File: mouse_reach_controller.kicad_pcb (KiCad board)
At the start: 2 copper layers, 158.8 x 57.2 mm, 83 parts, among them J1 AUDIO_JACK_3.5MM, P1 BNC_DOUBLE_RA, P2 BNC_DOUBLE_RA, P3 HEADER_02X05_LATCH, P4 HEADER_02X05_LATCH, P5 HEADER_02X05_LATCH, P6 PWR_JACK_2.1x5.5_SMD_RA, P7 BNC_DOUBLE_RA, T1 TERM_BLK_HDR_2POS_90DEG_0.2IN, T2 TERM_BLK_HDR_4POS_90DEG_0.2IN, U1 TMC429, U10 SGTL5000, U11 TMC424, U12 74LVC1G125GS, U13 74LVC1G125GS, U14 74LVC1G125GS, U15 74LVC1G125GS, U2 SN65LVDM050QDRQ1, U3 74LVC1G125GS, U4 SN65LVDM050QDRQ1, U5 74LVC1G125GS, U6 SN65LVDM050QDRQ1, U7 74LVC1G125GS, U8 DRV103, U9 RT9076-15GV

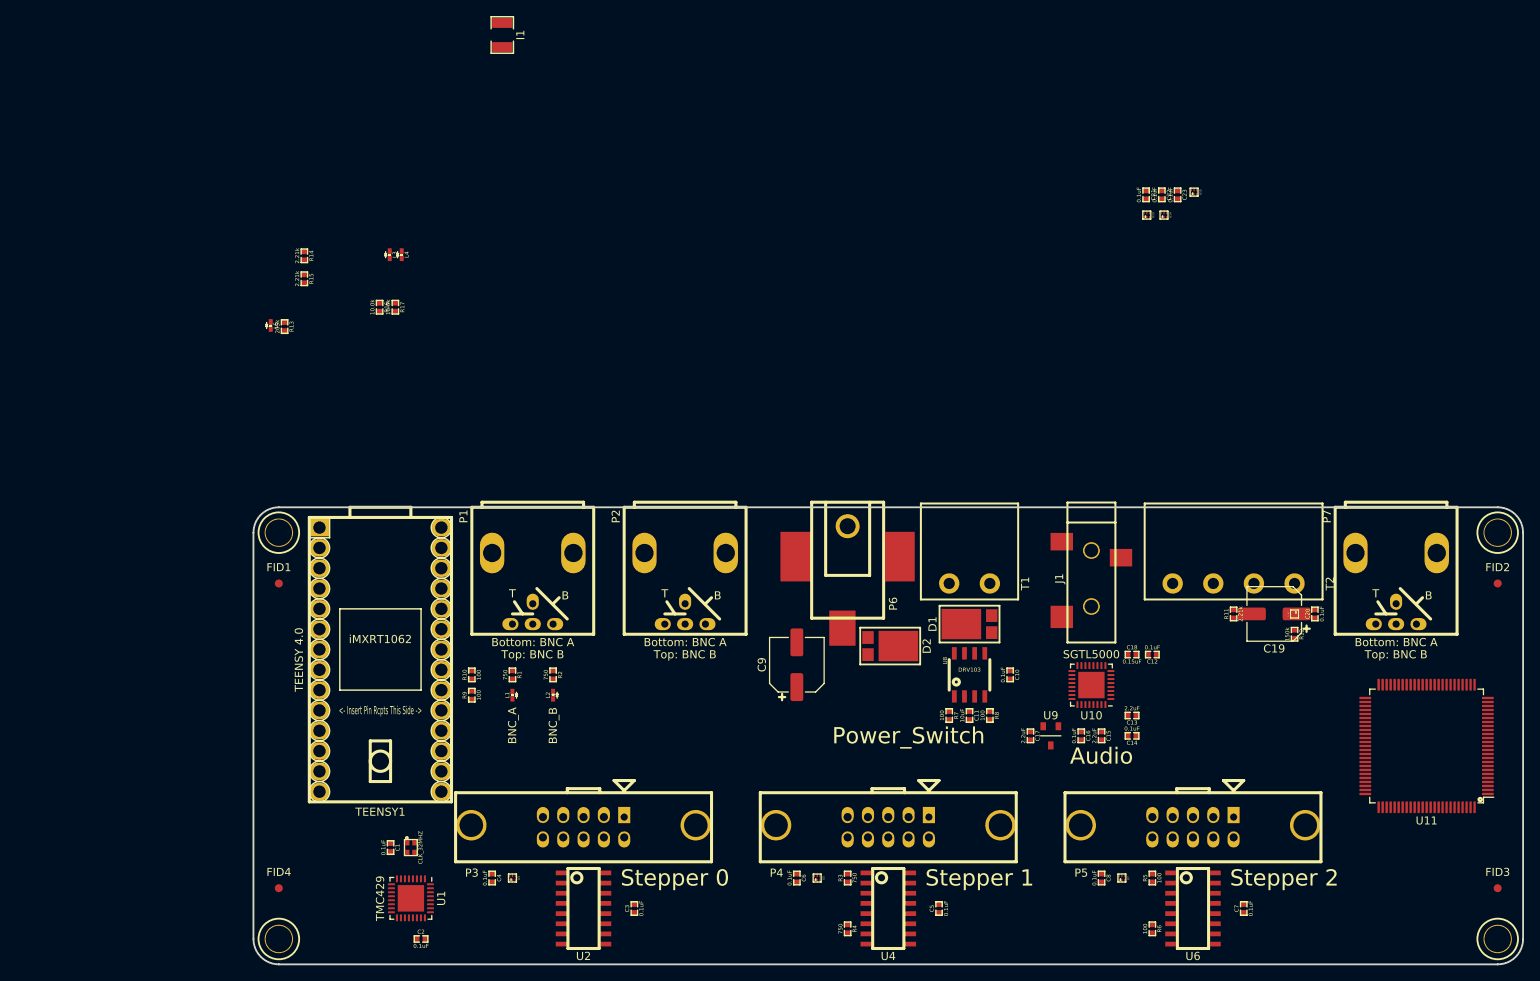
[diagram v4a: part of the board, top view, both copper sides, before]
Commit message: Update footprint text
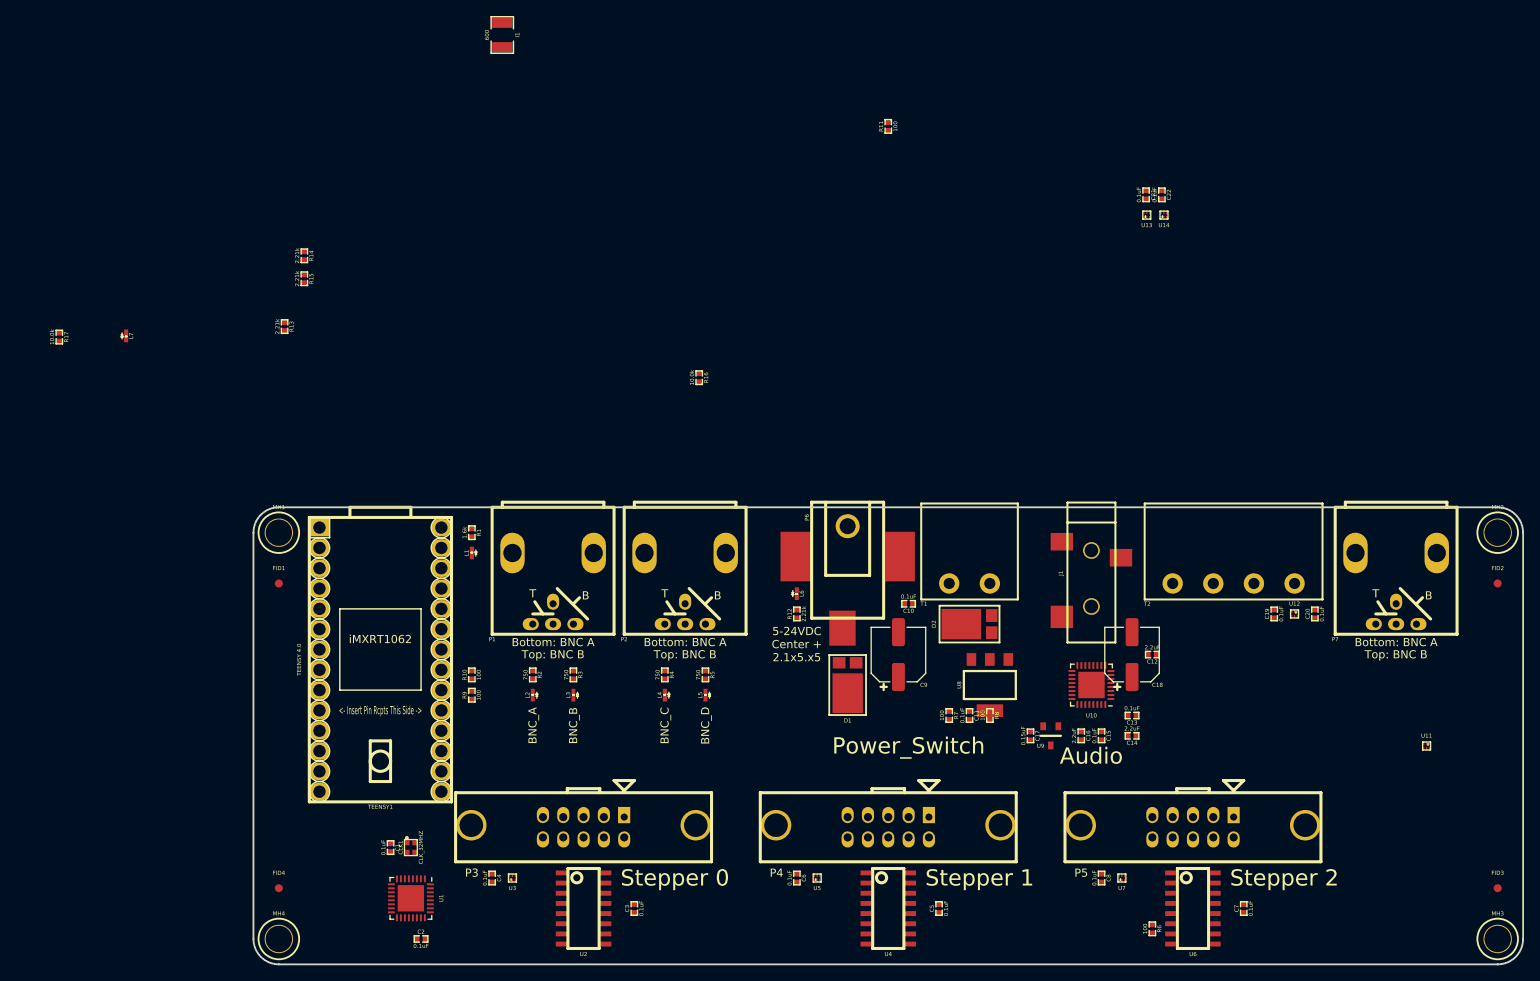
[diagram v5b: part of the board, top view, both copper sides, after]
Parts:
- removed C23: 0.1uF, mouse_reach_controller:SM0402
- removed U15: 74LVC1G125GS, mouse_reach_controller:SOT1202
- added L6: LED, mouse_reach_controller:LED_0402, F.Cu at (137.2, 62.2)
- added L7: LED, mouse_reach_controller:LED_0402, F.Cu at (53.3, 30.0)
- C11: value 10uF -> 0.1uF
- C12, C14, C16: value 0.1uF -> 2.2uF
- C13, C15: value 2.2uF -> 0.1uF
- C17: value 2.2uF -> 0.15uF
- C18: value 0.15uF -> 100uF_POL; footprint mouse_reach_controller:SM0402 -> mouse_reach_controller:CP_Elec_6.3x7.7_WURTH
- C19: value 100uF_POL -> 0.1uF; footprint mouse_reach_controller:CP_Elec_6.3x7.7_WURTH -> mouse_reach_controller:SM0402
- MH1, MH2, MH3, MH4: value MOUNTING_HOLE_4-40 -> VAL**
- R1: value 750 -> 1.6k
- R11: value 2.21k -> 100
- R12: value 150k -> 2.21k
- R13: value 205k -> 2.21k
- R5: value 100 -> 750
- T1: value TERM_BLK_HDR_2POS_90DEG_0.2IN -> VAL**
- T2: value TERM_BLK_HDR_4POS_90DEG_0.2IN -> VAL**
- TEENSY1: value TEENSY_4.0_PIN_RECEPTACLES -> VAL**
- U11: value TMC424 -> 74LVC1G125GS; footprint mouse_reach_controller:TQFP-100_14x14mm_P0.5mm -> mouse_reach_controller:SOT1202
- U8: value DRV103 -> ZXMS6006SG; footprint mouse_reach_controller:SOIC_8 -> mouse_reach_controller:SOT-223-3
- moved R11 74.7 mm to (148.6, 3.81)
- moved L5 71.4 mm to (125.7, 74.9), turned to 180 degrees
- moved L4 64.2 mm to (120.7, 74.9), turned to 180 degrees
- moved R12 62.3 mm to (137.2, 64.8), turned to 180 degrees
- moved R5 61.4 mm to (125.7, 72.4), turned to 0 degrees
- moved L3 59.7 mm to (109.2, 74.9), turned to 180 degrees
- moved R3 42.7 mm to (109.2, 72.4), turned to 0 degrees
- moved R17 42.2 mm to (44.9, 30.1)
- moved R16 40.9 mm to (124.9, 35.2)
- moved R4 39.1 mm to (120.7, 72.4)
- moved L1 18.5 mm to (96.5, 57.1)
- moved R1 18.5 mm to (96.5, 54.6)
- moved D1 17.0 mm to (143.5, 73.7), turned to 0 degrees
- moved C10 15.5 mm to (151.1, 63.5), turned to 270 degrees
- moved C9 12.8 mm to (149.9, 69.8)
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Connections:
- C11 pad 1: Net-(C11-Pad1) -> /VDD
- C12 pad 1: /VDD -> Net-(C12-Pad1)
- C13 pad 1: Net-(C13-Pad1) -> Net-(C12-Pad1)
- C14 pad 1: Net-(C13-Pad1) -> /VDD
- C16 pad 1: /VDD -> /audio_controller/VEE
- C17 pad 1: /audio_controller/VEE -> /audio_controller/VAG
- C18 pad 1: /audio_controller/VAG -> /VCC
- C19 pad 1: /VCC -> /VDD
- I1 pad 2: Net-(C13-Pad1) -> Net-(C12-Pad1)
- L5 pad 1: /power_switch_driver/OUT -> /GND
- R1 pad 1: /BNC_A -> /VCC
- R10 pad 1: /stepper_controller/stepper_driver_interface_2/REFR_A -> /stepper_controller/stepper_driver_interface_2/REF_A
- R10 pad 2: /stepper_controller/stepper_driver_interface_2/REFR_B -> /stepper_controller/stepper_driver_interface_2/REF_B
- R11 pad 1: /power_switch_driver/VBB -> /stepper_controller/stepper_driver_interface_2/REFR_A
- R11 pad 2: Net-(L5-Pad2) -> /stepper_controller/stepper_driver_interface_2/REFR_B
- R12 pad 1: Net-(R12-Pad1) -> /power_switch_driver/VAA
- R12 pad 2: /GND -> Net-(L6-Pad2)
- R13 pad 1: Net-(R13-Pad1) -> /power_switch_driver/VBB
- R13 pad 2: /GND -> Net-(L7-Pad2)
- R2 pad 1: /BNC_B -> /BNC_A
- R3 pad 1: /BNC_C -> /BNC_B
- R4 pad 1: /BNC_D -> /BNC_C
- R5 pad 1: /stepper_controller/stepper_driver_interface_0/REF_A -> /BNC_D
- R5 pad 2: /stepper_controller/stepper_driver_interface_0/REF_B -> Net-(L5-Pad2)
- R6 pad 1: /stepper_controller/stepper_driver_interface_0/REFR_A -> /stepper_controller/stepper_driver_interface_0/REF_A
- R6 pad 2: /stepper_controller/stepper_driver_interface_0/REFR_B -> /stepper_controller/stepper_driver_interface_0/REF_B
- R7 pad 1: /stepper_controller/stepper_driver_interface_1/REF_A -> /stepper_controller/stepper_driver_interface_0/REFR_A
- R7 pad 2: /stepper_controller/stepper_driver_interface_1/REF_B -> /stepper_controller/stepper_driver_interface_0/REFR_B
- R8 pad 1: /stepper_controller/stepper_driver_interface_1/REFR_A -> /stepper_controller/stepper_driver_interface_1/REF_A
- R8 pad 2: /stepper_controller/stepper_driver_interface_1/REFR_B -> /stepper_controller/stepper_driver_interface_1/REF_B
- R9 pad 1: /stepper_controller/stepper_driver_interface_2/REF_A -> /stepper_controller/stepper_driver_interface_1/REFR_A
- R9 pad 2: /stepper_controller/stepper_driver_interface_2/REF_B -> /stepper_controller/stepper_driver_interface_1/REFR_B
- U10 pad 5: Net-(C13-Pad1) -> Net-(C12-Pad1)
- U11 pad 1: (no net) -> /GND
- U11 pad 2: (no net) -> /ENCODER_A
- U11 pad 3: (no net) -> /GND
- U11 pad 6: (no net) -> /VDD
- U12 pad 2: /ENCODER_A -> /ENCODER_B
- U13 pad 2: /ENCODER_B -> /ENCODER_A
- U13 pad 4: (no net) -> /encoder_interface/CHANNEL_A_OUT
- U14 pad 2: /ENCODER_A -> /ENCODER_B
- U14 pad 4: /encoder_interface/CHANNEL_A_OUT -> /encoder_interface/CHANNEL_B_OUT
- U8 pad 1: Net-(R12-Pad1) -> /POWER_SWITCH_ENABLE
- U8 pad 2: Net-(C11-Pad1) -> /power_switch_driver/OUT
- U8 pad 3: Net-(R13-Pad1) -> /GND
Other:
- board text added: "5-24VDC Center + 2.1x5.x5"
- board text added: "BNC_C"
- board text added: "BNC_D"

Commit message: Create signal_interface sheet
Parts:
- added C23: 0.1uF, mouse_reach_controller:SM0402, F.Cu at (229.9, 20.3)
- added C24: 0.1uF, mouse_reach_controller:SM0402, F.Cu at (231.8, 20.3)
- added C25: 0.1uF, mouse_reach_controller:SM0402, F.Cu at (233.8, 20.3)
- added C26: 0.1uF, mouse_reach_controller:SM0402, F.Cu at (217.4, 20.3)
- added C27: 0.1uF, mouse_reach_controller:SM0402, F.Cu at (219.4, 20.3)
- added C28: 0.1uF, mouse_reach_controller:SM0402, F.Cu at (221.3, 20.3)
- added C29: 0.1uF, mouse_reach_controller:SM0402, F.Cu at (223.3, 20.3)
- added C30: 0.1uF, mouse_reach_controller:SM0402, F.Cu at (262.9, 33.0)
- added C31: 0.1uF, mouse_reach_controller:SM0402, F.Cu at (253.0, 32.9)
- added C32: 0.1uF, mouse_reach_controller:SM0402, F.Cu at (264.4, 30.1)
- added C33: 0.1uF, mouse_reach_controller:SM0402, F.Cu at (260.9, 33.0)
- added C34: 0.1uF, mouse_reach_controller:SM0402, F.Cu at (258.9, 33.0)
- added C35: 0.1uF, mouse_reach_controller:SM0402, F.Cu at (262.4, 30.1)
- added C36: 0.1uF, mouse_reach_controller:SM0402, F.Cu at (260.5, 30.1)
- added C37: 0.1uF, mouse_reach_controller:SM0402, F.Cu at (257.0, 33.0)
- added C38: 0.1uF, mouse_reach_controller:SM0402, F.Cu at (255.0, 33.0)
- added C39: 0.1uF, mouse_reach_controller:SM0402, F.Cu at (258.5, 30.1)
- added C40: 0.1uF, mouse_reach_controller:SM0402, F.Cu at (256.5, 30.1)
- added C41: 0.1uF, mouse_reach_controller:SM0402, F.Cu at (269.8, 30.1)
- added C42: 0.1uF, mouse_reach_controller:SM0402, F.Cu at (269.8, 33.0)
- added C43: 0.1uF, mouse_reach_controller:SM0402, F.Cu at (271.7, 30.1)
- added C44: 0.1uF, mouse_reach_controller:SM0402, F.Cu at (273.7, 30.1)
- added CLK2: CLK_16MHZ, mouse_reach_controller:XTAL_WURTH, F.Cu at (254.0, 30.1)
- added R18: 1.6k, mouse_reach_controller:SM0402, F.Cu at (271.7, 33.0)
- added R19: 1.6k, mouse_reach_controller:SM0402, F.Cu at (273.7, 33.0)
- added R20: 1.6k, mouse_reach_controller:SM0402, F.Cu at (275.7, 30.1)
- added U15: 74LVC1G125GS, mouse_reach_controller:SOT1202, F.Cu at (235.9, 20.0)
- added U16: 74LVC1G125GS, mouse_reach_controller:SOT1202, F.Cu at (217.5, 22.9)
- added U17: 74LVC1G125GS, mouse_reach_controller:SOT1202, F.Cu at (219.6, 22.9)
- added U18: 74LVC1G125GS, mouse_reach_controller:SOT1202, F.Cu at (221.8, 22.9)
- added U19: 74LVC1G125GS, mouse_reach_controller:SOT1202, F.Cu at (223.9, 22.9)
- added U20: 74LVC1G125GS, mouse_reach_controller:SOT1202, F.Cu at (277.7, 29.8)
- C19, C21: value 0.1uF -> 2.2uF
- MH1, MH2, MH3, MH4: value VAL** -> MOUNTING_HOLE_4-40
- P1, P2: value BNC_DOUBLE_RA -> HEADER_02X05_LATCH; footprint mouse_reach_controller:BNC_DOUBLE -> mouse_reach_controller:HEADER_02x05_LATCH
- P4: value HEADER_02X05_LATCH -> PWR_JACK_2.1x5.5_SMD_RA; footprint mouse_reach_controller:HEADER_02x05_LATCH -> mouse_reach_controller:DCJACK_3PAD_SMD_RA
- P5: value HEADER_02X05_LATCH -> BNC_DOUBLE_RA; footprint mouse_reach_controller:HEADER_02x05_LATCH -> mouse_reach_controller:BNC_DOUBLE
- P6: value PWR_JACK_2.1x5.5_SMD_RA -> BNC_DOUBLE_RA; footprint mouse_reach_controller:DCJACK_3PAD_SMD_RA -> mouse_reach_controller:BNC_DOUBLE
- R10, R11, R8, R9: value 100 -> 2.21k
- R12, R13, R14, R15: value 2.21k -> 10.0k
- R17: value 10.0k -> 1.6k
- R2, R3, R4, R5: value 750 -> 100
- T1: value VAL** -> TERM_BLK_HDR_2POS_90DEG_0.2IN
- T2: value VAL** -> TERM_BLK_HDR_4POS_90DEG_0.2IN
- TEENSY1: value VAL** -> TEENSY_4.0_PIN_RECEPTACLES
- U11: value 74LVC1G125GS -> RT9076-15GV; footprint mouse_reach_controller:SOT1202 -> mouse_reach_controller:SOT-23-3
- U14: value 74LVC1G125GS -> TMC424; footprint mouse_reach_controller:SOT1202 -> mouse_reach_controller:TQFP-100_14x14mm_P0.5mm
- moved P3 92.7 mm to (203.2, 91.4)
- moved P7 87.6 mm to (124.5, 57.1)
- moved R9 53.1 mm to (106.7, 22.9)
- moved R10 53.1 mm to (106.7, 20.3)
- moved P2 49.4 mm to (158.8, 91.4)
- moved P5 42.7 mm to (212.1, 57.1)
- moved P4 41.0 mm to (143.5, 50.8)
- moved P6 37.4 mm to (106.7, 57.1)
- moved P1 35.1 mm to (114.3, 91.4)
- moved C7 16.5 mm to (209.6, 101.6)
- moved C8 16.5 mm to (191.8, 97.8)
- moved R6 16.5 mm to (198.1, 104.1)
- moved U6 16.5 mm to (203.2, 101.6)
- moved U7 16.5 mm to (194.3, 97.8)
- moved U5 10.2 mm to (149.9, 97.8)
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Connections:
- net /~CS renamed /~STEPPER_CS
- C21 pad 1: /VDD -> /encoder_interface/VEE
- L3 pad 1: /GND -> /power_switch_driver/OUT
- L7 pad 1: /power_switch_driver/OUT -> /GND
- P1 pad 1: /BNC_A -> /stepper_controller/stepper_driver_interface_0/STEP_A
- P1 pad 2: /GND -> /stepper_controller/stepper_driver_interface_0/STEP_B
- P1 pad 3: /BNC_B -> /stepper_controller/stepper_driver_interface_0/DIR_A
- P1 pad 4: /GND -> /stepper_controller/stepper_driver_interface_0/DIR_B
- P2 pad 1: /BNC_C -> /stepper_controller/stepper_driver_interface_1/STEP_A
- P2 pad 2: /GND -> /stepper_controller/stepper_driver_interface_1/STEP_B
- P2 pad 3: /BNC_D -> /stepper_controller/stepper_driver_interface_1/DIR_A
- P2 pad 4: /GND -> /stepper_controller/stepper_driver_interface_1/DIR_B
- P3 pad 1: /stepper_controller/stepper_driver_interface_0/STEP_A -> /stepper_controller/stepper_driver_interface_2/STEP_A
- P3 pad 10: /stepper_controller/stepper_driver_interface_0/REFR_B -> /stepper_controller/stepper_driver_interface_2/REFR_B
- P3 pad 2: /stepper_controller/stepper_driver_interface_0/STEP_B -> /stepper_controller/stepper_driver_interface_2/STEP_B
- P3 pad 3: /stepper_controller/stepper_driver_interface_0/DIR_A -> /stepper_controller/stepper_driver_interface_2/DIR_A
- P3 pad 4: /stepper_controller/stepper_driver_interface_0/DIR_B -> /stepper_controller/stepper_driver_interface_2/DIR_B
- P3 pad 5: /stepper_controller/stepper_driver_interface_0/UART_BUFFERED -> /stepper_controller/stepper_driver_interface_2/UART_BUFFERED
- P3 pad 7: /stepper_controller/stepper_driver_interface_0/REF_A -> /stepper_controller/stepper_driver_interface_2/REF_A
- P3 pad 8: /stepper_controller/stepper_driver_interface_0/REF_B -> /stepper_controller/stepper_driver_interface_2/REF_B
- P3 pad 9: /stepper_controller/stepper_driver_interface_0/REFR_A -> /stepper_controller/stepper_driver_interface_2/REFR_A
- P4 pad 1: /stepper_controller/stepper_driver_interface_1/STEP_A -> /power_switch_driver/VAA
- P4 pad 2: /stepper_controller/stepper_driver_interface_1/STEP_B -> /GND
- P4 pad 3: /stepper_controller/stepper_driver_interface_1/DIR_A -> (no net)
- P5 pad 1: /stepper_controller/stepper_driver_interface_2/STEP_A -> /encoder_interface/CHANNEL_A_OUT
- P5 pad 2: /stepper_controller/stepper_driver_interface_2/STEP_B -> /GND
- P5 pad 3: /stepper_controller/stepper_driver_interface_2/DIR_A -> /encoder_interface/CHANNEL_B_OUT
- P5 pad 4: /stepper_controller/stepper_driver_interface_2/DIR_B -> /GND
- P6 pad 1: /power_switch_driver/VAA -> /signal_interface/SIGNAL_A_BUF
- P6 pad 3: (no net) -> /signal_interface/SIGNAL_B_BUF
- P7 pad 1: /encoder_interface/CHANNEL_A_OUT -> /signal_interface/SIGNAL_C_BUF
- P7 pad 3: /encoder_interface/CHANNEL_B_OUT -> /signal_interface/SIGNAL_D_BUF
- R10 pad 1: /stepper_controller/stepper_driver_interface_2/REF_A -> /VDD
- R10 pad 2: /stepper_controller/stepper_driver_interface_2/REF_B -> /SDA
- R11 pad 1: /stepper_controller/stepper_driver_interface_2/REFR_A -> /VDD
- R11 pad 2: /stepper_controller/stepper_driver_interface_2/REFR_B -> /SCL
- R12 pad 1: /power_switch_driver/VAA -> /VDD
- R12 pad 2: Net-(L6-Pad2) -> Net-(R12-Pad2)
- R13 pad 1: /power_switch_driver/VBB -> /VDD
- R13 pad 2: Net-(L7-Pad2) -> Net-(R13-Pad2)
- R14 pad 2: /SDA -> /encoder_interface/CHANNEL_A
- R15 pad 2: /SCL -> /encoder_interface/CHANNEL_B
- R16 pad 2: /ENCODER_A -> /encoder_interface/VDD_PULLUP
- R17 pad 1: /VDD -> /signal_interface/SIGNAL_A_BUF
- R17 pad 2: /ENCODER_B -> Net-(L4-Pad2)
- R2 pad 1: /BNC_A -> /stepper_controller/stepper_driver_interface_0/REF_A
- R2 pad 2: Net-(L2-Pad2) -> /stepper_controller/stepper_driver_interface_0/REF_B
- R3 pad 1: /BNC_B -> /stepper_controller/stepper_driver_interface_0/REFR_A
- R3 pad 2: Net-(L3-Pad2) -> /stepper_controller/stepper_driver_interface_0/REFR_B
- R4 pad 1: /BNC_C -> /stepper_controller/stepper_driver_interface_1/REF_A
- R4 pad 2: Net-(L4-Pad2) -> /stepper_controller/stepper_driver_interface_1/REF_B
- R5 pad 1: /BNC_D -> /stepper_controller/stepper_driver_interface_1/REFR_A
- R5 pad 2: Net-(L5-Pad2) -> /stepper_controller/stepper_driver_interface_1/REFR_B
- R6 pad 1: /stepper_controller/stepper_driver_interface_0/REF_A -> /stepper_controller/stepper_driver_interface_2/REF_A
- R6 pad 2: /stepper_controller/stepper_driver_interface_0/REF_B -> /stepper_controller/stepper_driver_interface_2/REF_B
- R7 pad 1: /stepper_controller/stepper_driver_interface_0/REFR_A -> /stepper_controller/stepper_driver_interface_2/REFR_A
- R7 pad 2: /stepper_controller/stepper_driver_interface_0/REFR_B -> /stepper_controller/stepper_driver_interface_2/REFR_B
- R8 pad 1: /stepper_controller/stepper_driver_interface_1/REF_A -> /power_switch_driver/VAA
- R8 pad 2: /stepper_controller/stepper_driver_interface_1/REF_B -> Net-(L2-Pad2)
- R9 pad 1: /stepper_controller/stepper_driver_interface_1/REFR_A -> /power_switch_driver/VBB
- R9 pad 2: /stepper_controller/stepper_driver_interface_1/REFR_B -> Net-(L3-Pad2)
- T2 pad 3: /ENCODER_A -> /encoder_interface/CHANNEL_A
- T2 pad 4: /ENCODER_B -> /encoder_interface/CHANNEL_B
- TEENSY1 pad 15: (no net) -> /ENCODER_INVERT
- TEENSY1 pad 2: /BNC_A -> /SIGNAL_A
- TEENSY1 pad 3: /BNC_B -> /SIGNAL_B
- TEENSY1 pad 4: /BNC_C -> /SIGNAL_C
- TEENSY1 pad 5: /BNC_D -> /SIGNAL_D
- TEENSY1 pad 6: /ENCODER_A -> /~ENCODER_RESET
- TEENSY1 pad 9: /ENCODER_B -> /~ENCODER_CS
- U11 pad 1: /GND -> /VDD
- U11 pad 2: /ENCODER_A -> /encoder_interface/VEE
- U12 pad 2: /ENCODER_B -> /encoder_interface/CHANNEL_A
- U12 pad 4: (no net) -> /encoder_interface/CHANNEL_A_TMC424
- U13 pad 2: /ENCODER_A -> /encoder_interface/CHANNEL_B
- U13 pad 4: /encoder_interface/CHANNEL_A_OUT -> /encoder_interface/CHANNEL_B_TMC424
- U14 pad 2: /ENCODER_B -> (no net)
- U14 pad 3: /GND -> /encoder_interface/CHANNEL_A_TMC424
- U14 pad 4: /encoder_interface/CHANNEL_B_OUT -> /encoder_interface/CHANNEL_B_TMC424
- U14 pad 5: (no net) -> /encoder_interface/VDD_PULLUP
- U14 pad 6: /VDD -> /encoder_interface/VDD_PULLUP

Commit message: Progress towards v1.1 pcb layout
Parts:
- I1: footprint mouse_reach_controller:SM1210 -> mouse_reach_controller:SM0402
- TEENSY1: value TEENSY_4.0_PIN_RECEPTACLES -> VAL**
- moved C41 174.7 mm to (101.6, 77.5), turned to 90 degrees
- moved R18 169.7 mm to (106.7, 72.4), turned to 90 degrees
- moved C42 169.0 mm to (106.7, 77.5), turned to 90 degrees
- moved U20 159.8 mm to (124.5, 74.9), turned to 90 degrees
- moved C43 159.5 mm to (119.4, 77.5), turned to 90 degrees
- moved R19 159.3 mm to (119.4, 72.4), turned to 90 degrees
- moved R20 157.0 mm to (124.5, 72.4), turned to 90 degrees
- moved C44 156.6 mm to (124.5, 77.5), turned to 90 degrees
- moved U17 129.0 mm to (101.6, 74.9), turned to 90 degrees
- moved U18 126.3 mm to (106.7, 74.9), turned to 90 degrees
- moved U19 116.8 mm to (119.4, 74.9), turned to 90 degrees
- moved U14 100.0 mm to (274.3, 55.9)
- moved I1 94.3 mm to (167.6, 58.4), turned to 90 degrees
- moved R11 86.5 mm to (95.9, 72.4)
- moved L7 85.0 mm to (127.0, 72.4), turned to 90 degrees
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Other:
- board text added: "Encoder"
- board text added: "Power Switch"
- board text added: "SIGNAL A"
- board text added: "SIGNAL B"
- board text added: "SIGNAL C"
- board text added: "SIGNAL D"
- board text added: "Signals"
- board text added: "mouse_reach_controller Janelia Research Campus 12/2021 ver 1.1"
- board text removed: "BNC_A"
- board text removed: "BNC_B"
- board text removed: "BNC_C"
- board text removed: "BNC_D"
- board text removed: "Power_Switch"
- board text removed: "mouse_reach_controller Janelia Research Campus 11/2021 ver 1.1"

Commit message: Route board
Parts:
- moved R13 160.1 mm to (224.8, 80.0), turned to 90 degrees
- moved R14 156.2 mm to (224.8, 66.0), turned to 270 degrees
- moved R15 154.6 mm to (224.8, 63.5), turned to 270 degrees
- moved C21 91.5 mm to (219.7, 95.2), turned to 270 degrees
- moved R16 87.8 mm to (204.5, 72.4), turned to 90 degrees
- moved C39 83.1 mm to (193.0, 81.3), turned to 90 degrees
- moved C40 78.6 mm to (196.8, 81.3), turned to 90 degrees
- moved C35 73.7 mm to (213.4, 85.1)
- moved R12 73.0 mm to (221.0, 85.1), turned to 0 degrees
- moved U15 72.7 mm to (193.0, 78.7), turned to 90 degrees
- moved C36 72.0 mm to (224.8, 92.7), turned to 90 degrees
- moved C22 71.0 mm to (204.5, 80.0), turned to 270 degrees
- moved C34 70.3 mm to (204.5, 77.5), turned to 270 degrees
- moved C33 70.3 mm to (204.5, 74.9), turned to 270 degrees
- moved C19 67.7 mm to (219.7, 105.4), turned to 270 degrees
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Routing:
- net /GND: track 0.00 -> 798.4 mm, vias 0 -> 19
- net /VDD: track 0.00 -> 505.7 mm, vias 0 -> 15
- net /VCC: track 0.00 -> 186.9 mm, vias 0 -> 3
- net /MOSI: track 0.00 -> 163.8 mm, vias 0 -> 2
- net /MISO: track 0.00 -> 163.7 mm, vias 0 -> 2
- net /~ENCODER_RESET: track 0.00 -> 163.3 mm, vias 0 -> 1
- net /SCK: track 0.00 -> 148.2 mm, vias 0 -> 2
- net /ENCODER_INVERT: track 0.00 -> 147.4 mm, vias 0 -> 2
- net /~ENCODER_CS: track 0.00 -> 145.5 mm
- net /stepper_controller/REF_2: track 0.00 -> 125.4 mm, vias 0 -> 2
- net /stepper_controller/REFR_2: track 0.00 -> 120.0 mm, vias 0 -> 2
- net /I2S_DIN: track 0.00 -> 117.6 mm, vias 0 -> 1
- net /I2S_DOUT: track 0.00 -> 115.0 mm, vias 0 -> 1
- net /UART_2: track 0.00 -> 112.2 mm, vias 0 -> 1
- net /stepper_controller/STEP_2: track 0.00 -> 111.5 mm
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- added copper zone on B.Cu, net /GND
- added copper zone on F.Cu, net /GND
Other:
- net class THICKPOWER: clearance 0.2032 -> 0.1016; trace_width 1.524 -> 0.6096; via_dia 1.524 -> 0.635; via_drill 0.635 -> 0.4064
- net class THICKSIGNAL: clearance 0.2032 -> 0.1016; via_dia 0.9144 -> 0.635; via_drill 0.635 -> 0.4064
- board text added: "A"
- board text added: "B"
- board text added: "GND"
- board text added: "V+"
